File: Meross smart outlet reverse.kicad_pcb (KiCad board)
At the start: 2 copper layers, 63 parts, among them CN1 Conn_01x01, CN2 Conn_01x01, CN3 Conn_01x01, K1 G2RL-1A-H, Q1 MMBT3904, SW1 SW_SPST, U1 OB2222M, U2 LM317L_SOT-89, U3 CSE7759B

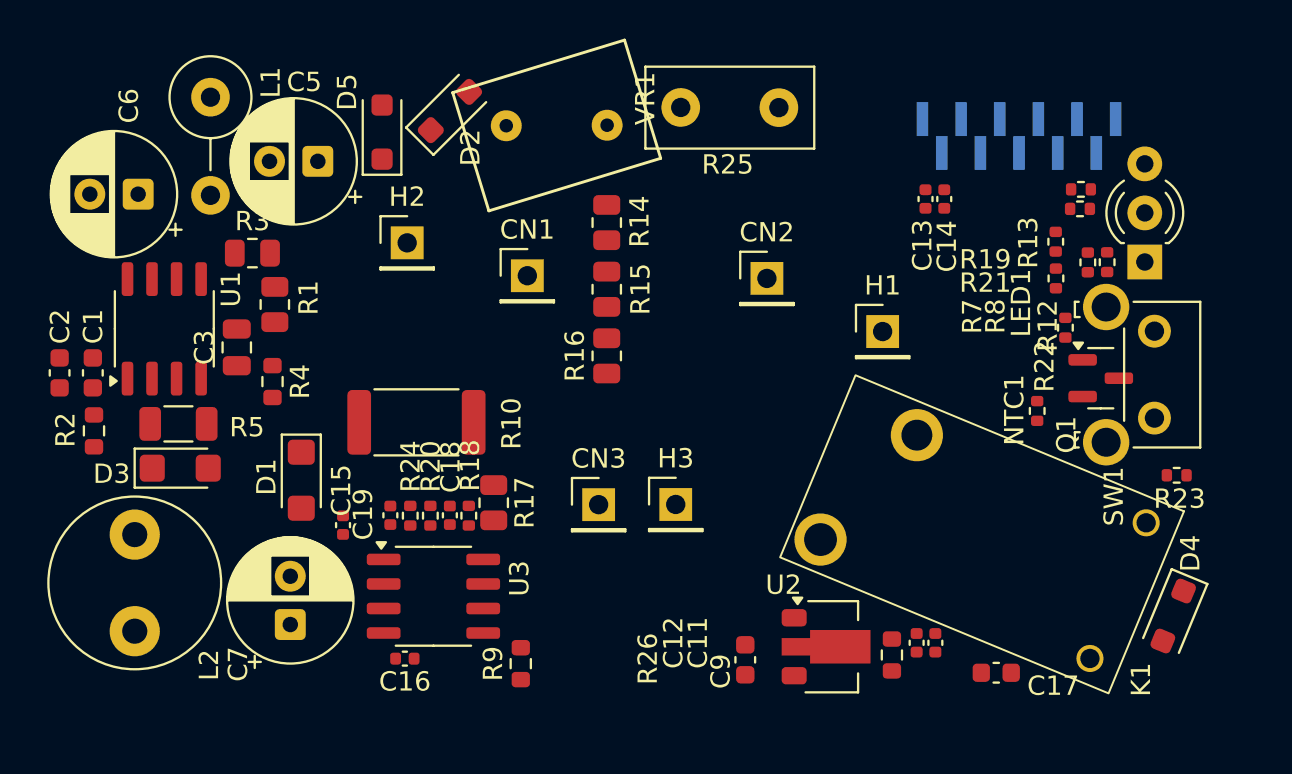
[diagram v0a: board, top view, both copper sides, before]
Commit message: Have a full board layout which resembles the original in some ways. Made a few schematic fixes to match better.
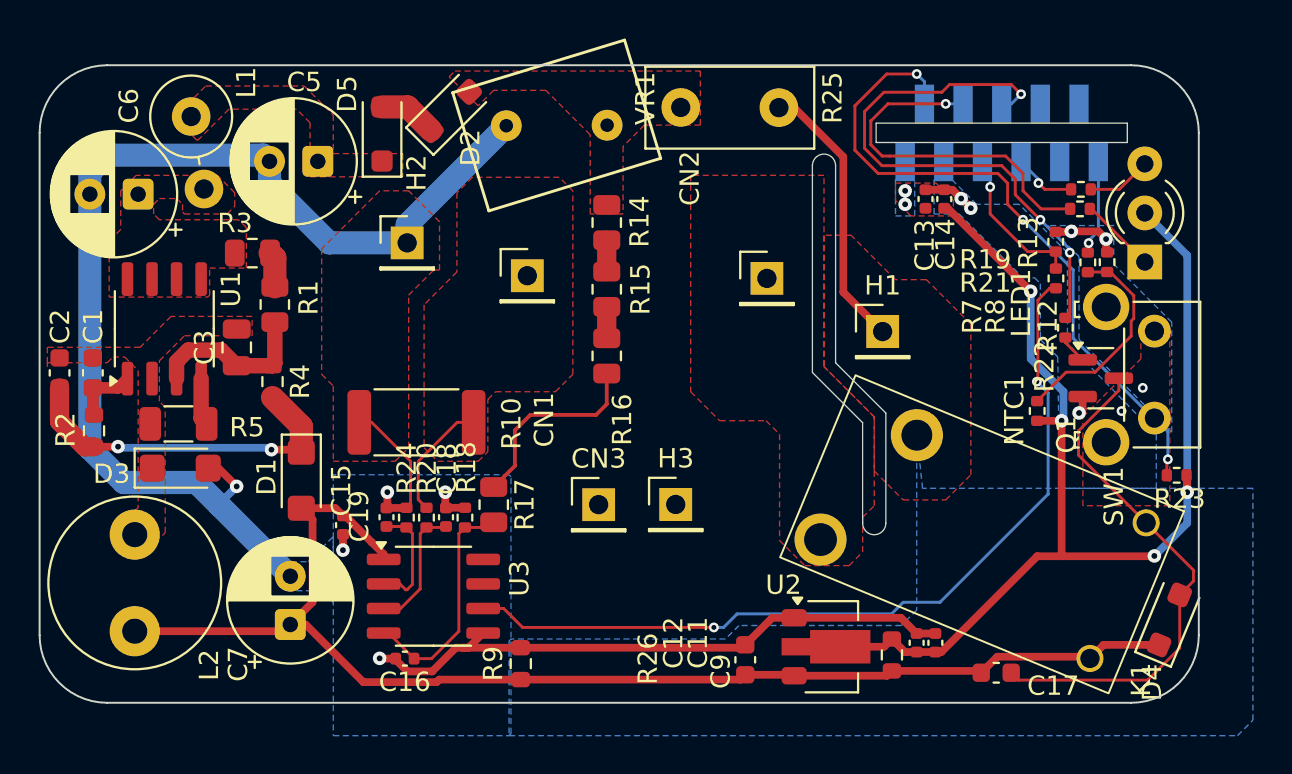
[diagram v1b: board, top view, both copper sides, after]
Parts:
- L1: footprint Inductor_THT:L_Axial_L9.5mm_D4.0mm_P5.08mm_Vertical_Fastron_SMCC -> HF relays:L_Axial_L9.5mm_D4.0mm_P3.81mm_Vertical
- MC1: footprint Connector_PinHeader_1.00mm:PinHeader_1x11_P1.00mm_Vertical_SMD_Pin1Left -> HF relays:BoardToBoardInterface_11xP1.00mm
- moved L1 1.41 mm to (129.8, 86.2), turned to -80 degrees
- moved MC1 0.91 mm to (171.8, 87.0)
- moved D4 0.28 mm to (180.5, 112.2), turned to 67.5 degrees
- moved R18 0.22 mm to (144.0, 106.9)
- moved C18 0.22 mm to (143.0, 106.9)
- moved R20 0.22 mm to (142.0, 106.9)
- moved R24 0.22 mm to (141.0, 106.9)
- moved C19 0.22 mm to (140.0, 106.9)
- moved D5 0.10 mm to (139.7, 87.1)
- moved R17 0.10 mm to (145.5, 106.2)
- turned C13 to -90 degrees
- turned C14 to -90 degrees
- turned C16 to 180 degrees
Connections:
- net C renamed /Power Supplies/HV_DC
- net Net-(D5-K) renamed /Power Supplies/RECT_AC
- K1 pad A1: +5V -> Net-(D4-A)
- K1 pad A2: Net-(D4-A) -> +5V
- MC1 pad 2: POWER_EN -> /Microcontroller/~{BUTTON}
- MC1 pad 6: Net-(MC1-Pin_6) -> POWER_EN
- R20 pad 2: Net-(U3-V1P) -> Net-(U3-V1N)
- R23 pad 2: POWER_EN -> /Microcontroller/~{BUTTON}
- R24 pad 2: Net-(U3-V1N) -> Net-(U3-V1P)
- SW1 pad 1: Net-(MC1-Pin_6) -> NEUTRAL_SRC
- SW1 pad 2: NEUTRAL_SRC -> /Microcontroller/~{BUTTON}
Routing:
- net NEUTRAL_SRC: track 0.00 -> 107.7 mm, vias 0 -> 12
- net +5V: track 0.00 -> 67.6 mm
- net +3V3: track 0.00 -> 63.3 mm, vias 0 -> 6
- net /current measurement/MEAS_SER_5V: track 0.00 -> 44.0 mm, vias 0 -> 2
- net /Microcontroller/~{BUTTON}: track 0.00 -> 35.1 mm, vias 0 -> 3
- net POWER_EN: track 0.00 -> 28.9 mm, vias 0 -> 3
- net Net-(D4-A): track 0.00 -> 27.2 mm
- net ~{LED_RED}: track 0.00 -> 18.6 mm, vias 0 -> 1
- net Net-(D1-K): track 0.00 -> 18.4 mm, vias 0 -> 2
- net LINE_IN: track 0.00 -> 14.3 mm
- net /current measurement/DIV_VOLTAGE: track 0.00 -> 12.1 mm
- net Net-(NTC1-Pad1): track 0.00 -> 11.3 mm
- net Net-(R16-Pad1): track 0.00 -> 10.3 mm
- net Net-(U1-VDD): track 0.00 -> 8.73 mm
- net MEAS_SER: track 0.00 -> 7.95 mm, vias 0 -> 1
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- added copper zone on B.Cu, net +3V3
- added copper zone on F.Cu, net +3V3
- added copper zone on F.Cu, net /Power Supplies/HV_DC
- added copper zone on F.Cu, net /Power Supplies/RECT_AC
- added copper zone on F.Cu, net FUSED_AC
- added copper zone on F.Cu, net LINE_IN
- added copper zone on F.Cu, net LINE_OUT
- added copper zone on F.Cu, net NEUTRAL_LOAD
- added copper zone on B.Cu, net NEUTRAL_SRC
- added copper zone on F.Cu, net NEUTRAL_SRC
- added copper zone on F.Cu, net Net-(D3-K)
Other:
- board outline added: 60 x 33 mm

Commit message: Making board layout match better. Added new footprints and symbols.
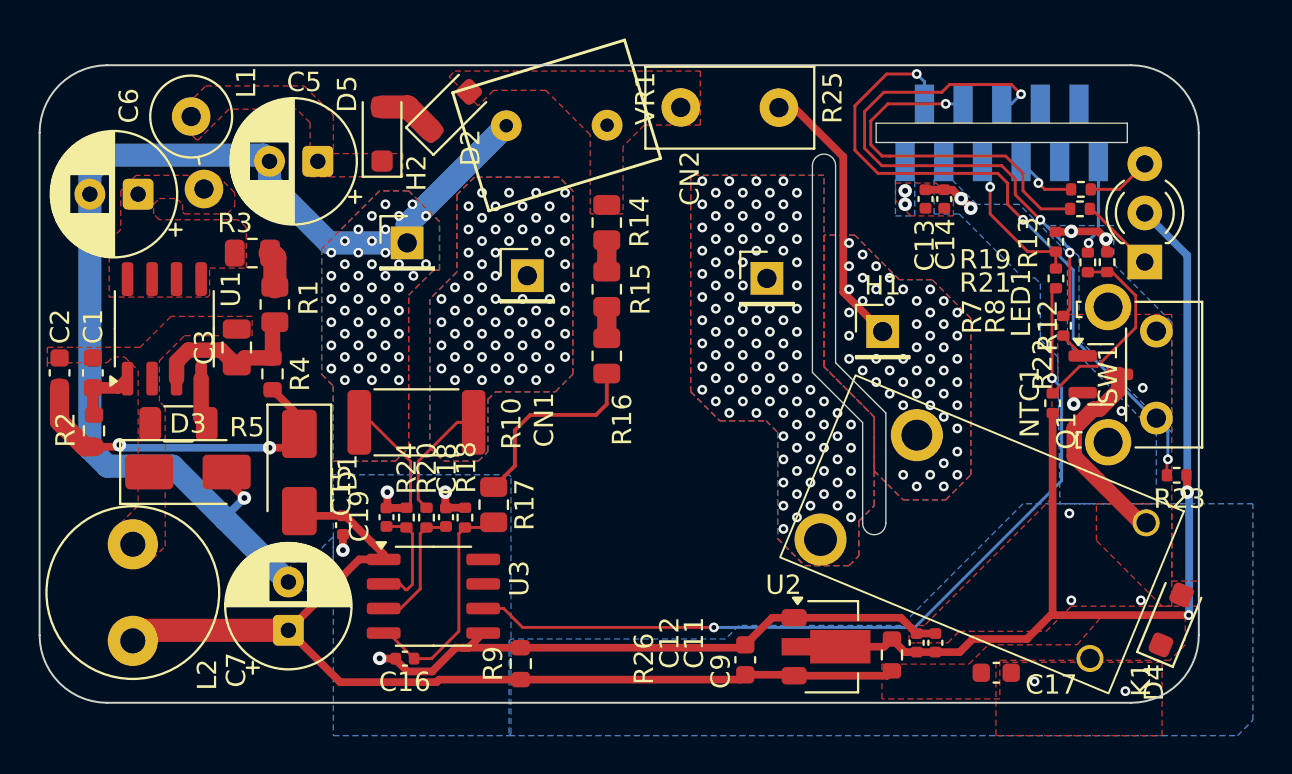
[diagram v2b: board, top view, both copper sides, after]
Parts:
- removed CN3, H3: Conn_01x01, Connector_PinHeader_2.54mm:PinHeader_1x01_P2.54mm_Vertical
- C1: value C -> 1µF
- C11: value C -> 3.3µF
- C12, C15: value C -> 100nF
- C16, C18, C19: value C -> 33nF
- C17, C9: value C -> 10µF
- C3: value C -> 4.7µF
- D1: value 1N4007 -> M7; footprint Diode_SMD:D_SMF -> Diode_SMD:D_SMA
- D3: footprint Diode_SMD:D_SMF -> Diode_SMD:D_SMA
- K1: value G2RL-1A-H -> HF32FV-16/5-HLTF(590)
- L2: value 470µ -> 470µH
- NTC1: value Thermistor_NTC_US -> 10kΩ
- R12: value 1KΩ -> 1kΩ
- R13: value 2KΩ -> 2kΩ
- R26: value R_US -> R
- R8: value R_US -> 10kΩ
- SW1: footprint Button_Switch_THT:SW_SPST_Omron_B3F-315x_Angled -> HF relays:SW_SPST_Omron_B3F-315x_Angled
- U2: value LM317L_SOT-89 -> STK17-3.3
- moved NTC1 0.89 mm to (174.4, 101.0)
- moved L2 0.51 mm to (126.8, 108.3)
- moved D3 0.45 mm to (129.7, 104.6)
- moved D1 0.41 mm to (135.4, 104.6)
- moved R4 0.40 mm to (134.1, 99.5)
- moved C7 0.32 mm to (134.9, 112.7)
- moved Q1 0.20 mm to (176.9, 99.5)
- moved R22 0.14 mm to (175.0, 97.0)
- moved D4 0.10 mm to (180.6, 112.2)
- moved SW1 0.10 mm to (179.8, 97.3)
- turned C17 to 0 degrees
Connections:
- net /Microcontroller/~{BUTTON} renamed /~{BUTTON}
- net Net-(D3-K) renamed /Power Supplies/U1_GND
- C17 pad 1: Net-(D4-A) -> +5V
- C17 pad 2: +5V -> NEUTRAL_SRC
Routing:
- net Net-(D4-A): track 27.2 -> 10.5 mm
- net +5V: track 67.6 -> 53.1 mm
- net +3V3: track 63.3 -> 54.9 mm, vias 6 -> 4
- net Net-(NTC1-Pad1): track 11.3 -> 10.4 mm
- net NEUTRAL_SRC: track 107.7 -> 106.8 mm, vias 12 -> 64
- net NEUTRAL_LOAD: vias 0 -> 69
- net LINE_OUT: vias 0 -> 108
- net LINE_IN: vias 0 -> 52
- added copper zone on F.Cu, net +5V
- added copper zone on B.Cu, net LINE_IN
- added copper zone on B.Cu, net LINE_OUT
- added copper zone on B.Cu, net NEUTRAL_LOAD
- added copper zone on F.Cu, net Net-(D4-A)

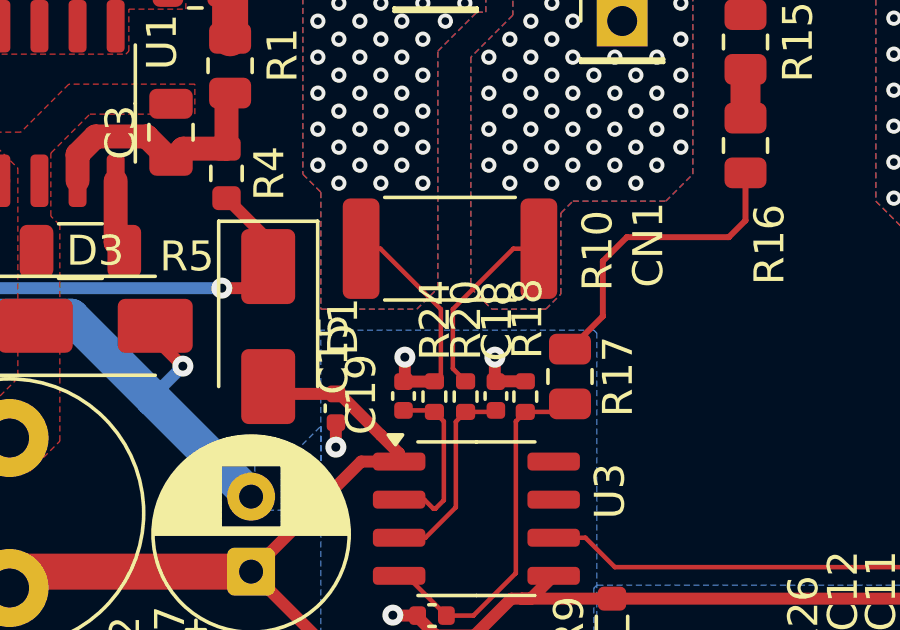
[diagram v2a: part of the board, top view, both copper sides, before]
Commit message: All values determined for schematic. From measurements, datasheets, or reading markings.
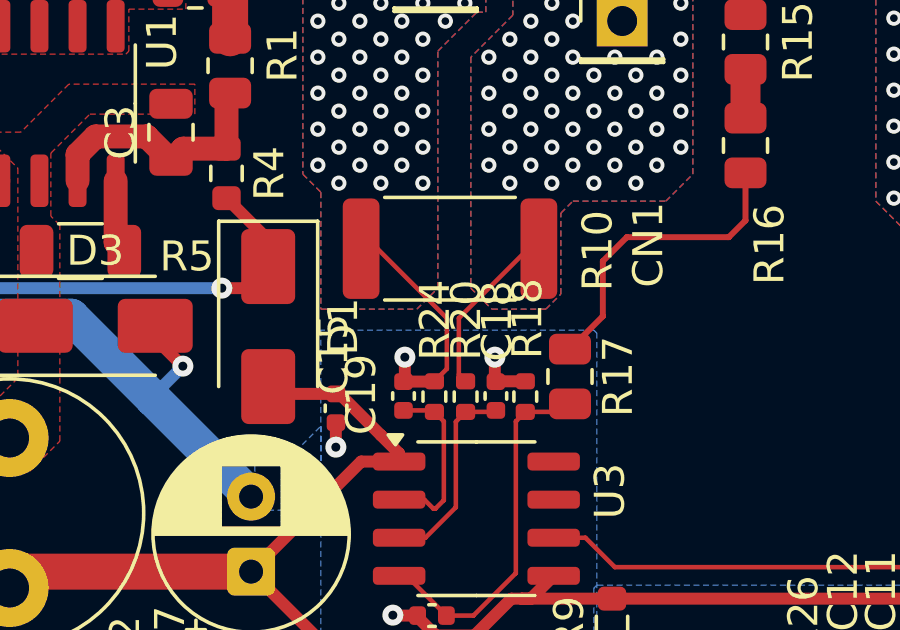
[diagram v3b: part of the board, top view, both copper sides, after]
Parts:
- D2, D5: value 1N4007 -> A7
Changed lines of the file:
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@@
 			)
 		)
-		(property "Value" "1N4007"
+		(property "Value" "A7"
 			(at 0 2.1 45)
 			(layer "F.Fab")
@@
 			)
 		)
-		(property "Value" "1N4007"
+		(property "Value" "A7"
 			(at 0 2.1 90)
 			(layer "F.Fab")
@@
 	)
 	(segment
+		(start 139.085 101.985)
+		(end 138.5425 101.985)
+		(width 0.1524)
+		(layer "F.Cu")
+		(net 4)
+	)
+	(segment
 		(start 177.2 93.13)
 		(end 177.255 93.185)
@@
 	)
 	(segment
+		(start 141.4 105.99)
+		(end 141.4 104.3)
+		(width 0.1524)
+		(layer "F.Cu")
+		(net 4)
+	)
+	(segment
 		(start 177.2 92.5)
 		(end 177.2 93.13)
@@
 	)
 	(segment
+		(start 140.985 106.405)
+		(end 141.4 105.99)
+		(width 0.1524)
+		(layer "F.Cu")
+		(net 4)
+	)
+	(segment
 		(start 175.4 92.1)
 		(end 176.8 92.1)
@@
 	)
 	(segment
-		(start 139.185 101.985)
-		(end 138.5425 101.985)
-		(width 0.1524)
-		(layer "F.Cu")
-		(net 4)
-	)
-	(segment
 		(start 142.3216 114.8784)
 		(end 143.55 113.65)
@@
 	)
 	(segment
-		(start 141.2 106.19)
-		(end 141.2 104)
-		(width 0.1524)
-		(layer "F.Cu")
-		(net 4)
-	)
-	(segment
 		(start 140.425 114.215)
 		(end 140.425 114.266654)
@@
 	)
 	(segment
-		(start 140.985 106.405)
-		(end 141.2 106.19)
-		(width 0.1524)
-		(layer "F.Cu")
-		(net 4)
-	)
-	(segment
 		(start 158.525 113.5)
 		(end 159.925 112.1)
@@
 	)
 	(segment
-		(start 143 106.38)
-		(end 143.035 106.415)
-		(width 0.4)
+		(start 141.4 104.3)
+		(end 139.085 101.985)
+		(width 0.1524)
 		(layer "F.Cu")
 		(net 4)
 	)
 	(segment
-		(start 141.2 104)
-		(end 139.185 101.985)
-		(width 0.1524)
+		(start 143 106.38)
+		(end 143.035 106.415)
+		(width 0.4)
 		(layer "F.Cu")
 		(net 4)
@@
 	)
 	(segment
-		(start 143.615 101.985)
-		(end 144.4675 101.985)
+		(start 141.8 106.18)
+		(end 141.8 104.3)
 		(width 0.1524)
 		(layer "F.Cu")
@@
 	)
 	(segment
-		(start 141.6 105.98)
-		(end 141.6 104)
+		(start 142.025 106.405)
+		(end 141.8 106.18)
 		(width 0.1524)
 		(layer "F.Cu")
@@
 	)
 	(segment
-		(start 141.6 104)
-		(end 143.615 101.985)
+		(start 144.115 101.985)
+		(end 144.4675 101.985)
 		(width 0.1524)
 		(layer "F.Cu")
@@
 	)
 	(segment
-		(start 142.025 106.405)
-		(end 141.6 105.98)
+		(start 141.8 104.3)
+		(end 144.115 101.985)
 		(width 0.1524)
 		(layer "F.Cu")
